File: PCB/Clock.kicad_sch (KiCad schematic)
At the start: 24 parts, among them SW1 SW_Push, SW2 SW_SPDT, U1 LM555xM, U2 LM555xM, U3 LM555xM, U4 74LS08, U5 74LS04, U6 74LS32

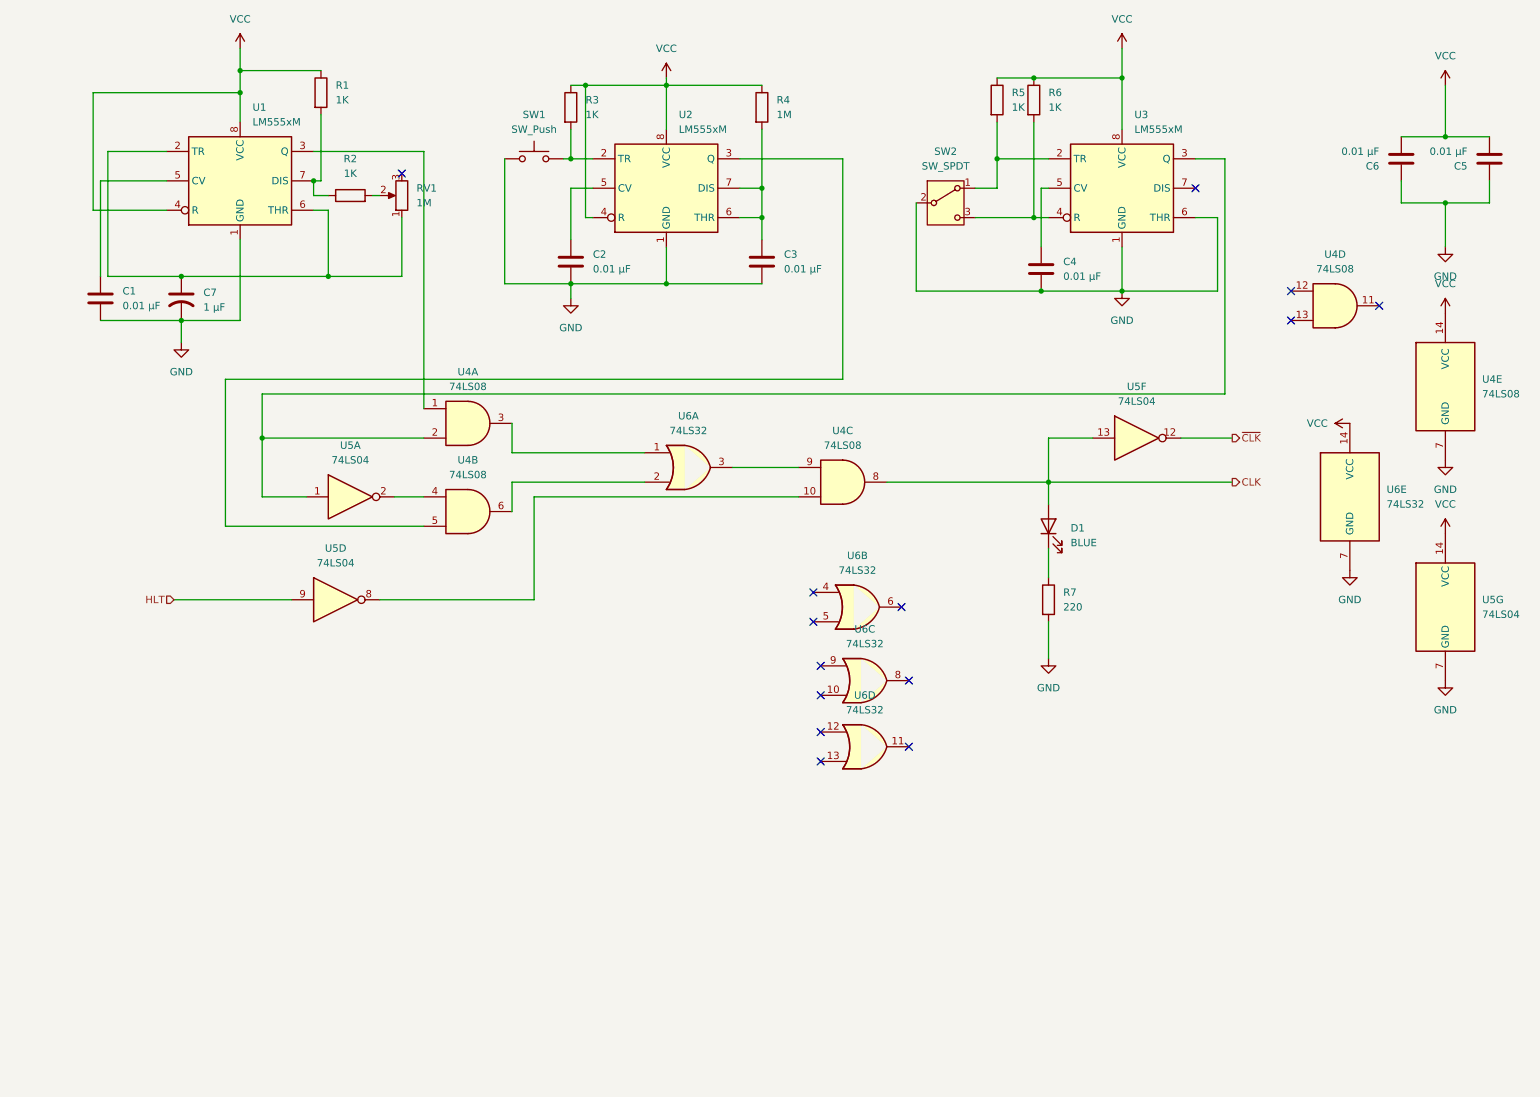
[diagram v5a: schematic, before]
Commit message: Add decupling caps and reroute pcb. Updated BOM to match new number of caps
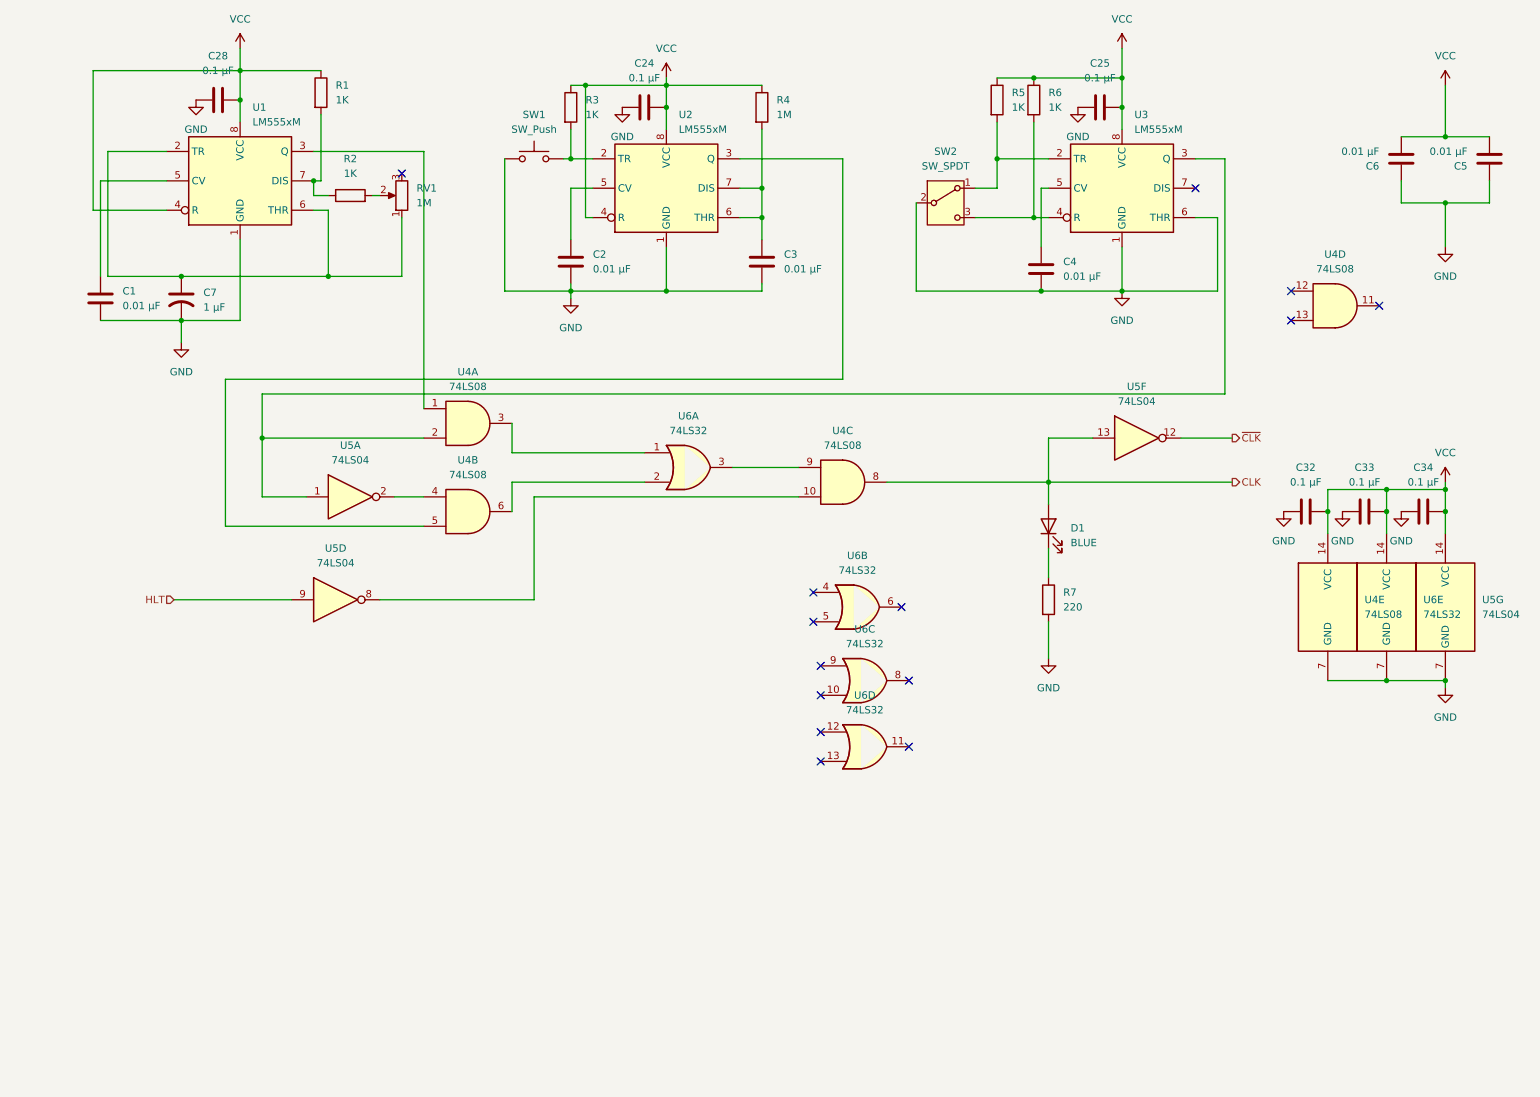
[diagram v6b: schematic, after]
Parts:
- added C24, C25, C28, C32, C33, C34: 0.1 µF, Capacitor_THT:C_Radial_D5.0mm_H5.0mm_P2.00mm, symbol Device:C
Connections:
- net GND: now also C24.2, C25.1, C28.1, C32.2, C33.1, C34.1
- net VCC: now also C24.1, C25.2, C28.2, C32.1, C33.2, C34.2
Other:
- moved on the sheet: U4E, U6E

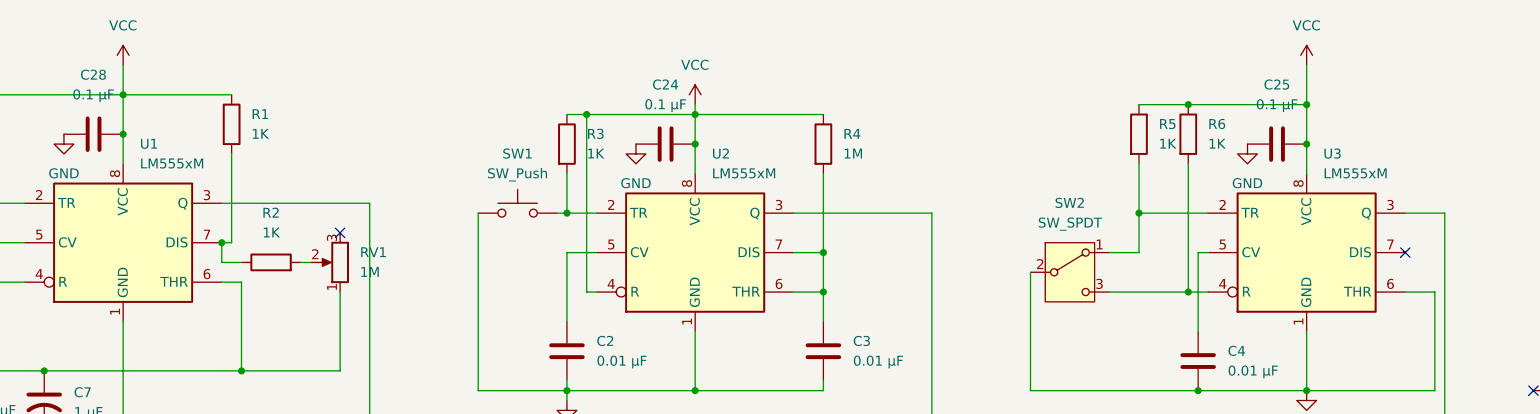
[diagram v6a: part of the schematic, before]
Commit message: Redoing PCB layout and fixed some signal flow convention errors
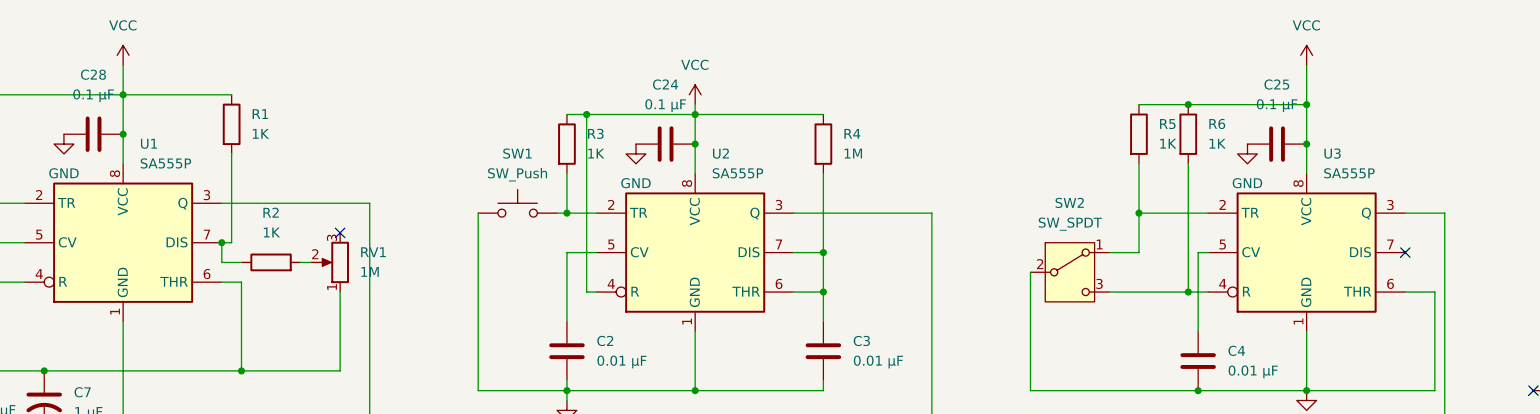
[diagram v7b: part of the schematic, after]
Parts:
- removed U1, U2, U3: LM555xM, Package_SO:SOIC-8_3.9x4.9mm_P1.27mm, symbol Timer:LM555xM
- added U1, U2, U3: SA555P, Package_DIP:DIP-8_W7.62mm, symbol Timer:SA555P
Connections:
- net GND: now also U1.1 (GND), U2.1 (GND), U3.1 (GND), U3.6 (THR)
- net VCC: now also U1.4 (R), U1.8 (VCC), U2.4 (R), U2.8 (VCC), U3.8 (VCC)
- net at C2.2: now also U2.5 (CV)
- net at C4.2: now also U3.5 (CV)
- net at U4.1: now also U1.3 (Q)
- net at U4.2, U5.1: now also U3.3 (Q)
- net at R6.2, SW2.3 (C): now also U3.4 (R)
- net at R5.2, SW2.1 (A): now also U3.2 (TR)
- net at C7.1, RV1.1: now also U1.2 (TR), U1.6 (THR)
- net at C1.2: now also U1.5 (CV)
- net at R1.2, R2.1: now also U1.7 (DIS)
- net at R3.2, SW1.2: now also U2.2 (TR)
- net at U4.5: now also U2.3 (Q)
- net at C3.2, R4.2: now also U2.6 (THR), U2.7 (DIS)
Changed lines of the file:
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@@
 	)
 	(symbol
+		(lib_id "Timer:SA555P")
+		(at 208.28 41.91 0)
+		(unit 1)
+		(exclude_from_sim no)
+		(in_bom yes)
+		(on_board yes)
+		(dnp no)
+		(fields_autoplaced yes)
+		(property "Reference" "U3"
+			(at 210.4233 29.21 0)
+			(effects
+				(font
+					(size 1.27 1.27)
+				)
+				(justify left)
+			)
+		)
+		(property "Value" "SA555P"
+			(at 210.4233 31.75 0)
+			(effects
+				(font
+					(size 1.27 1.27)
+				)
+				(justify left)
+			)
+		)
+		(property "Footprint" "Package_DIP:DIP-8_W7.62mm"
+			(at 224.79 52.07 0)
+			(effects
+				(font
+					(size 1.27 1.27)
+				)
+				(hide yes)
+			)
+		)
+		(property "Datasheet" "http://www.ti.com/lit/ds/symlink/ne555.pdf"
+			(at 229.87 52.07 0)
+			(effects
+				(font
+					(size 1.27 1.27)
+				)
+				(hide yes)
+			)
+		)
+		(property "Description" "Precision Timers, 555 compatible, PDIP-8"
+			(at 208.28 41.91 0)
+			(effects
+				(font
+					(size 1.27 1.27)
+				)
+				(hide yes)
+			)
+		)
+		(pin "6"
+		)
+		(pin "7"
+		)
+		(pin "3"
+		)
+		(pin "4"
+		)
+		(pin "5"
+		)
+		(pin "2"
+		)
+		(pin "1"
+		)
+		(pin "8"
+		)
+		(instances
+			(project "8-Bit-PC"
+				(path "/48633dea-2de9-4b6f-aeff-2ee54233f918/ab3d271b-f0b2-4c3a-a0c7-95dfaa179663"
+					(reference "U3")
+					(unit 1)
+				)
+			)
+		)
+	)
+	(symbol
 		(lib_id "Device:C")
 		(at 113.03 54.61 180)
@@
 	)
 	(symbol
-		(lib_id "Timer:LM555xM")
-		(at 208.28 41.91 0)
-		(unit 1)
-		(exclude_from_sim no)
-		(in_bom yes)
-		(on_board yes)
-		(dnp no)
-		(fields_autoplaced yes)
-		(property "Reference" "U3"
-			(at 210.4233 29.21 0)
-			(effects
-				(font
-					(size 1.27 1.27)
-				)
-				(justify left)
-			)
-		)
-		(property "Value" "LM555xM"
-			(at 210.4233 31.75 0)
-			(effects
-				(font
-					(size 1.27 1.27)
-				)
-				(justify left)
-			)
-		)
-		(property "Footprint" "Package_SO:SOIC-8_3.9x4.9mm_P1.27mm"
-			(at 229.87 52.07 0)
-			(effects
-				(font
-					(size 1.27 1.27)
-				)
-				(hide yes)
-			)
-		)
-		(property "Datasheet" "http://www.ti.com/lit/ds/symlink/lm555.pdf"
-			(at 229.87 52.07 0)
-			(effects
-				(font
-					(size 1.27 1.27)
-				)
-				(hide yes)
-			)
-		)
-		(property "Description" "Timer, 555 compatible, SOIC-8"
-			(at 208.28 41.91 0)
-			(effects
-				(font
-					(size 1.27 1.27)
-				)
-				(hide yes)
-			)
-		)
-		(pin "4"
-		)
-		(pin "3"
-		)
-		(pin "6"
-		)
-		(pin "7"
-		)
-		(pin "5"
-		)
-		(pin "2"
-		)
-		(pin "1"
-		)
-		(pin "8"
-		)
-		(instances
-			(project "8-Bit-PC"
-				(path "/48633dea-2de9-4b6f-aeff-2ee54233f918/ab3d271b-f0b2-4c3a-a0c7-95dfaa179663"
-					(reference "U3")
-					(unit 1)
-				)
-			)
-		)
-	)
-	(symbol
 		(lib_id "power:GND")
 		(at 195.58 123.19 0)
@@
 	)
 	(symbol
-		(lib_id "Timer:LM555xM")
-		(at 55.88 40.64 0)
-		(unit 1)
-		(exclude_from_sim no)
-		(in_bom yes)
-		(on_board yes)
-		(dnp no)
-		(fields_autoplaced yes)
-		(property "Reference" "U1"
-			(at 58.0233 27.94 0)
-			(effects
-				(font
-					(size 1.27 1.27)
-				)
-				(justify left)
-			)
-		)
-		(property "Value" "LM555xM"
-			(at 58.0233 30.48 0)
-			(effects
-				(font
-					(size 1.27 1.27)
-				)
-				(justify left)
-			)
-		)
-		(property "Footprint" "Package_SO:SOIC-8_3.9x4.9mm_P1.27mm"
-			(at 77.47 50.8 0)
-			(effects
-				(font
-					(size 1.27 1.27)
-				)
-				(hide yes)
-			)
-		)
-		(property "Datasheet" "http://www.ti.com/lit/ds/symlink/lm555.pdf"
-			(at 77.47 50.8 0)
-			(effects
-				(font
-					(size 1.27 1.27)
-				)
-				(hide yes)
-			)
-		)
-		(property "Description" "Timer, 555 compatible, SOIC-8"
-			(at 55.88 40.64 0)
-			(effects
-				(font
-					(size 1.27 1.27)
-				)
-				(hide yes)
-			)
-		)
-		(pin "4"
-		)
-		(pin "3"
-		)
-		(pin "6"
-		)
-		(pin "7"
-		)
-		(pin "5"
-		)
-		(pin "2"
-		)
-		(pin "1"
-		)
-		(pin "8"
-		)
-		(instances
-			(project "8-Bit-PC"
-				(path "/48633dea-2de9-4b6f-aeff-2ee54233f918/ab3d271b-f0b2-4c3a-a0c7-95dfaa179663"
-					(reference "U1")
-					(unit 1)
-				)
-			)
-		)
-	)
-	(symbol
 		(lib_id "Device:C")
 		(at 250.19 97.79 90)
@@
 	)
 	(symbol
-		(lib_id "Timer:LM555xM")
+		(lib_id "Timer:SA555P")
 		(at 129.54 41.91 0)
 		(unit 1)
@@
 			)
 		)
-		(property "Value" "LM555xM"
+		(property "Value" "SA555P"
 			(at 131.6833 31.75 0)
 			(effects
@@
 			)
 		)
-		(property "Footprint" "Package_SO:SOIC-8_3.9x4.9mm_P1.27mm"
-			(at 151.13 52.07 0)
+		(property "Footprint" "Package_DIP:DIP-8_W7.62mm"
+			(at 146.05 52.07 0)
 			(effects
 				(font
@@
 			)
 		)
-		(property "Datasheet" "http://www.ti.com/lit/ds/symlink/lm555.pdf"
+		(property "Datasheet" "http://www.ti.com/lit/ds/symlink/ne555.pdf"
 			(at 151.13 52.07 0)
 			(effects
@@
 			)
 		)
-		(property "Description" "Timer, 555 compatible, SOIC-8"
+		(property "Description" "Precision Timers, 555 compatible, PDIP-8"
 			(at 129.54 41.91 0)
 			(effects
@@
 			)
 		)
-		(pin "4"
-		)
-		(pin "3"
-		)
 		(pin "6"
 		)
 		(pin "7"
 		)
+		(pin "3"
+		)
+		(pin "4"
+		)
 		(pin "5"
 		)
@@
 					(unit 1)
 				)
+			)
+		)
+	)
+	(symbol
+		(lib_id "Timer:SA555P")
+		(at 55.88 40.64 0)
+		(unit 1)
+		(exclude_from_sim no)
+		(in_bom yes)
+		(on_board yes)
+		(dnp no)
+		(fields_autoplaced yes)
+		(property "Reference" "U1"
+			(at 58.0233 27.94 0)
+			(effects
+				(font
+					(size 1.27 1.27)
+				)
+				(justify left)
+			)
+		)
+		(property "Value" "SA555P"
+			(at 58.0233 30.48 0)
+			(effects
+				(font
+					(size 1.27 1.27)
+				)
+				(justify left)
+			)
+		)
+		(property "Footprint" "Package_DIP:DIP-8_W7.62mm"
+			(at 72.39 50.8 0)
+			(effects
+				(font
+					(size 1.27 1.27)
+				)
+				(hide yes)
+			)
+		)
+		(property "Datasheet" "http://www.ti.com/lit/ds/symlink/ne555.pdf"
+			(at 77.47 50.8 0)
+			(effects
+				(font
+					(size 1.27 1.27)
+				)
+				(hide yes)
+			)
+		)
+		(property "Description" "Precision Timers, 555 compatible, PDIP-8"
+			(at 55.88 40.64 0)
+			(effects
+				(font
+					(size 1.27 1.27)
+				)
+				(hide yes)
+			)
+		)
+		(pin "6"
+		)
+		(pin "7"
+		)
+		(pin "3"
+		)
+		(pin "4"
+		)
+		(pin "5"
+		)
+		(pin "2"
+		)
+		(pin "1"
+		)
+		(pin "8"
+		)
+		(instances
+			(project ""
+				(path "/48633dea-2de9-4b6f-aeff-2ee54233f918/ab3d271b-f0b2-4c3a-a0c7-95dfaa179663"
+					(reference "U1")
+					(unit 1)
+				)

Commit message: update BOM to reflect cheaper prices and more acurate item ammounts, also worked on laying out the PCB.
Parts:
- SW2: footprint Button_Switch_SMD:SW_SPDT_CK_JS102011SAQN -> Button_Switch_THT:SW_Slide-03_Wuerth-WS-SLTV_10x2.5x6.4_P2.54mm
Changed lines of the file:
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@@
 			)
 		)
-		(property "Footprint" "Button_Switch_SMD:SW_SPDT_CK_JS102011SAQN"
+		(property "Footprint" "Button_Switch_THT:SW_Slide-03_Wuerth-WS-SLTV_10x2.5x6.4_P2.54mm"
 			(at 177.8 44.45 0)
 			(effects
